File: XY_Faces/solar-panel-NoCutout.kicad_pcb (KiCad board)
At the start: 4 copper layers, 83 x 98 mm, 25 parts, among them J1 CON-5040500591, J2 Conn_01x01, J3 Conn_01x01, J4 Conn_01x01, J5 Conn_01x01, U1 VEML7700, U2 MCP9808_DFN, U3 DRV2605LDGS

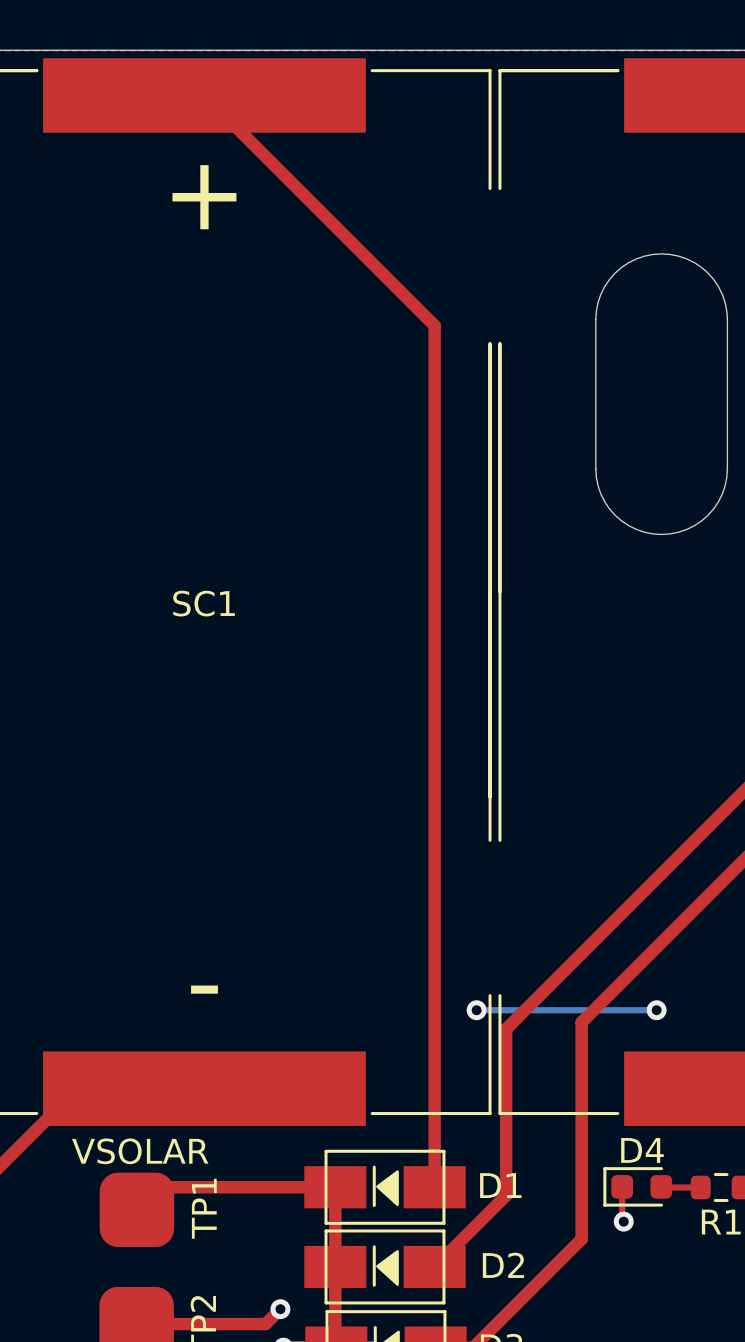
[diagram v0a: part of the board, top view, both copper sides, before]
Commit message: moved copper routing
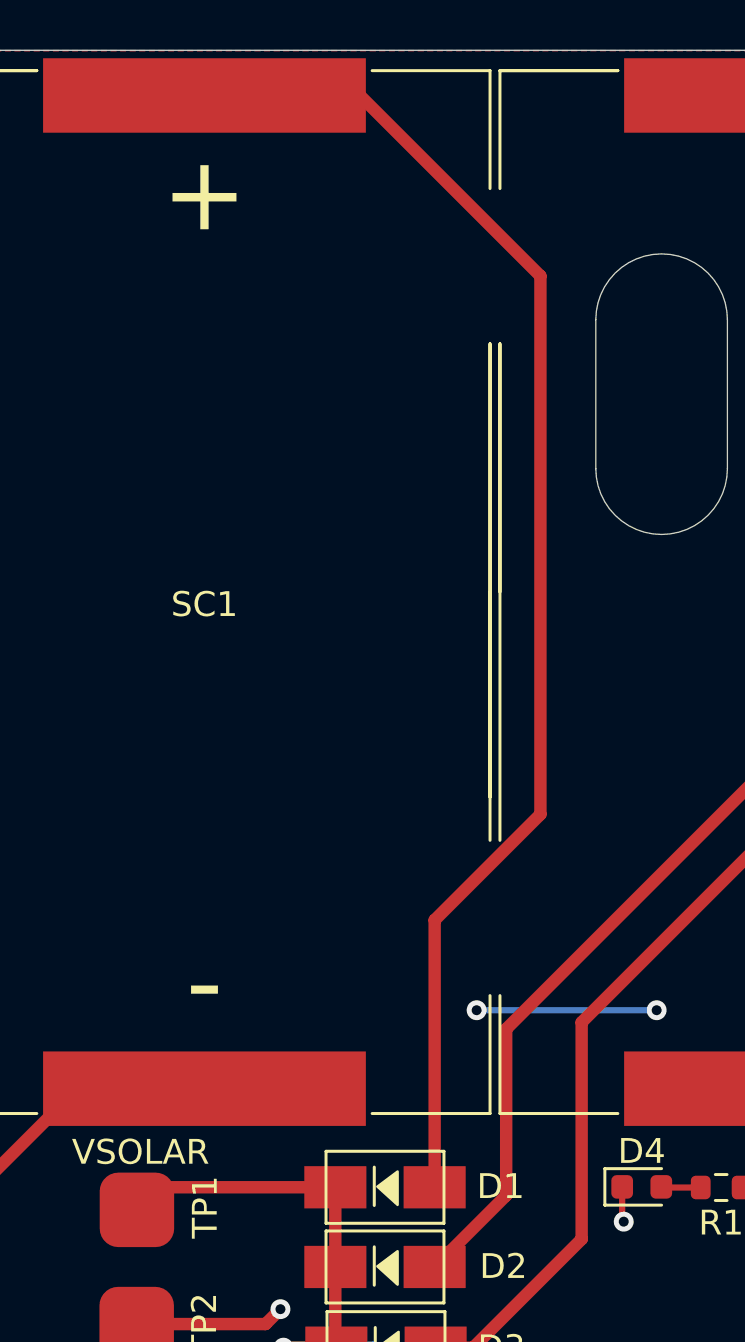
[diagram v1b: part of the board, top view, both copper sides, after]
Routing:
- net Net-(U3-Pad7): track 9246.2 -> 8719.1 mm
- net Net-(D1-Pad2): track 47.8 -> 55.0 mm
